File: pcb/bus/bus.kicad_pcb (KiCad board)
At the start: 4 copper layers, 117.4 x 100 mm, 35 parts, among them J201 Conn_02x10_Row_Letter_First, J301 Conn_02x10_Row_Letter_First, J401 Conn_02x10_Row_Letter_First, J501 Conn_02x10_Row_Letter_First, J601 Conn_02x10_Row_Letter_First, J701 Conn_02x10_Row_Letter_First, U101 USBLC6-2SC6, U102 FE1.1s, U103 USBLC6-2SC6, U104 USBLC6-2SC6, U105 USBLC6-2SC6, U106 USBLC6-2SC6, Y101 12MHz

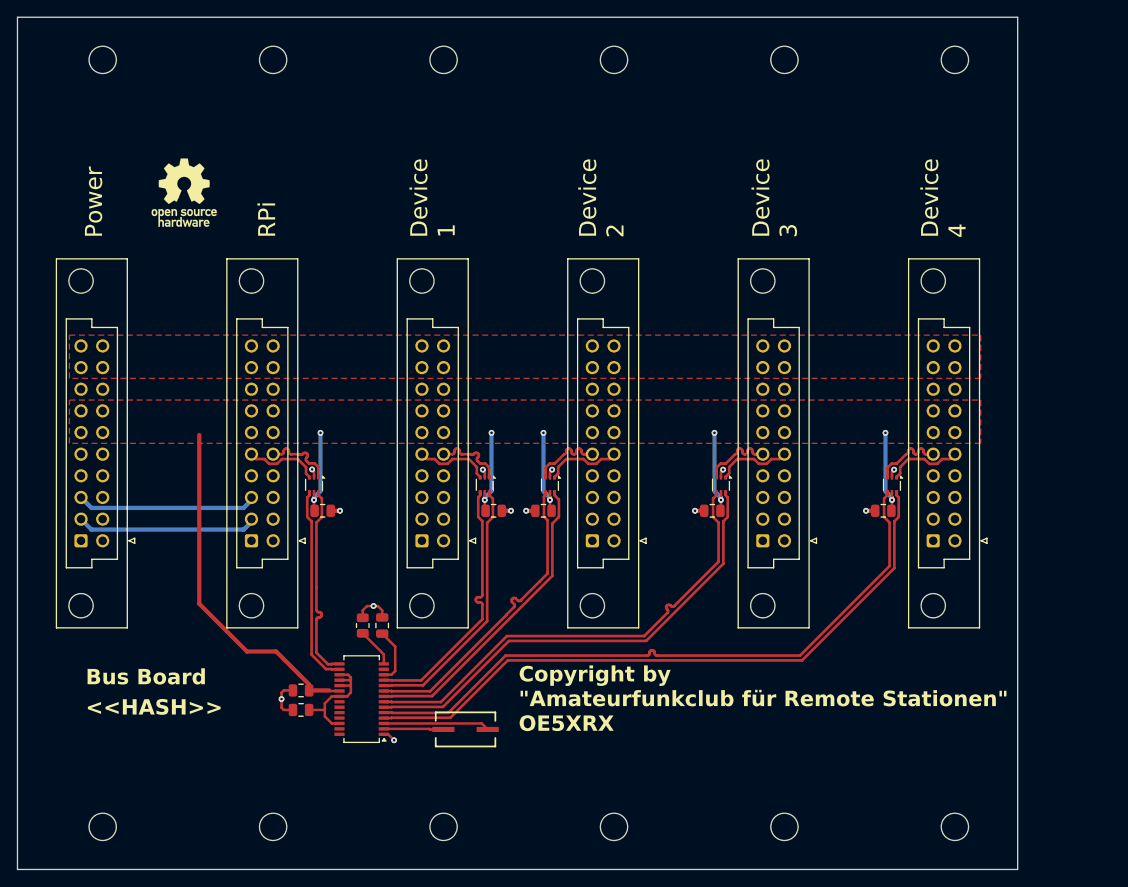
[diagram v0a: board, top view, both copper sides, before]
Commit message: move smd parts to backside - no usb length improvements
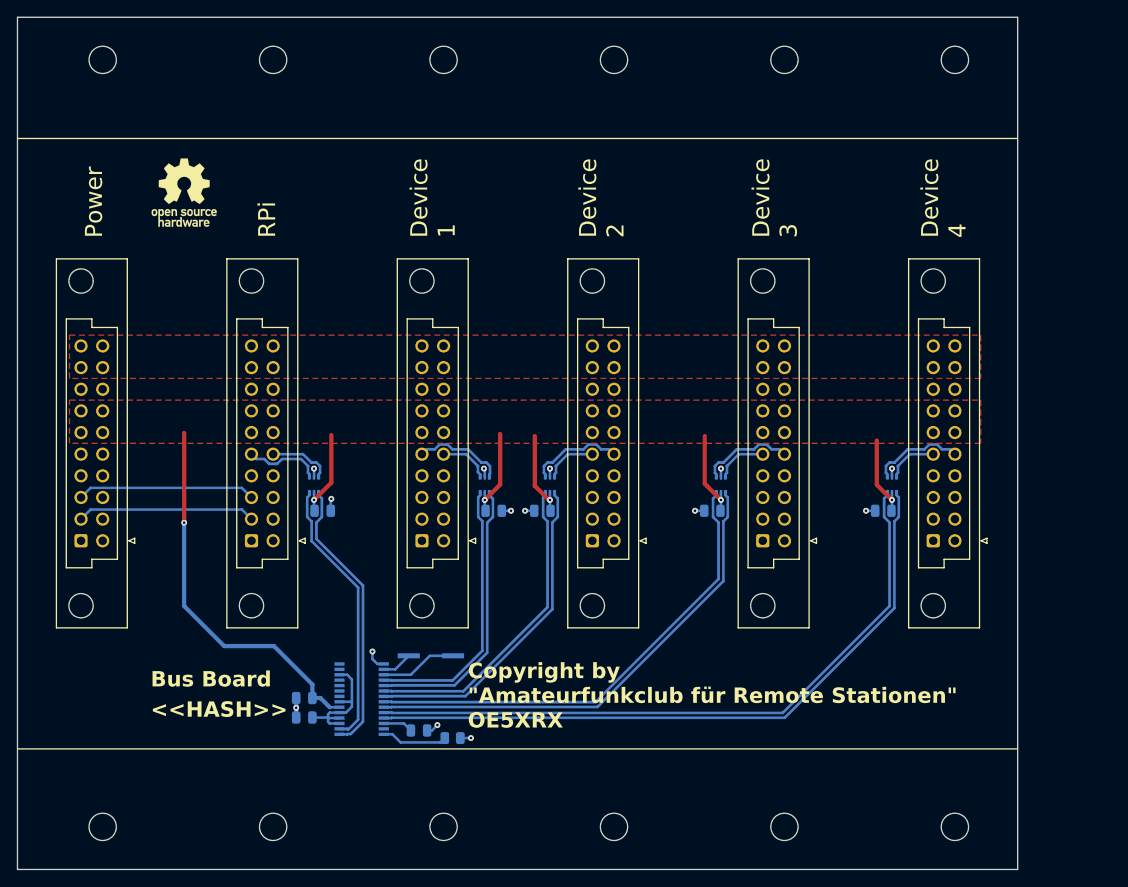
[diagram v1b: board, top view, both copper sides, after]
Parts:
- C101, C102, C103, C104, C105, C106, C107, C108, R103, U101, U102, U103, U104, U105, U106, Y101: moved to B.Cu
- moved R103 16.9 mm to (116.3, 110.0), turned to 0 degrees
- moved C102 13.1 mm to (112.4, 109.1), turned to 0 degrees
- moved Y101 9.54 mm to (113.8, 100.3)
- moved C101 0.97 mm to (98.9, 107.6)
- moved C103 0.97 mm to (98.9, 105.3)
- moved C106 0.13 mm to (126.9, 83.3)
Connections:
- U101 pad 1: /RPI Connector/NS_USB- -> /RPI Connector/NS_USB+
- U101 pad 3: /RPI Connector/NS_USB+ -> /RPI Connector/NS_USB-
- U101 pad 4: /MASTER_USB+ -> /MASTER_USB-
- U101 pad 6: /MASTER_USB- -> /MASTER_USB+
- U102 pad 10: /USB1- -> /USB4-
- U102 pad 11: /USB1+ -> /USB4+
- U102 pad 4: /USB4- -> /USB1-
- U102 pad 5: /USB4+ -> /USB1+
- U102 pad 6: /USB3- -> /USB2-
- U102 pad 7: /USB3+ -> /USB2+
- U102 pad 8: /USB2- -> /USB3-
- U102 pad 9: /USB2+ -> /USB3+
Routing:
- net /MASTER_USB-: track 23.3 -> 33.0 mm
- net /MASTER_USB+: track 23.4 -> 32.0 mm
- net +5V: track 89.9 -> 96.4 mm, vias 10 -> 6
- net Net-(U102-XIN): track 12.5 -> 9.05 mm
- net Net-(U102-XOUT): track 7.02 -> 3.59 mm
- net Net-(U102-REXT): track 4.71 -> 7.76 mm
- net /VD18: track 6.54 -> 3.52 mm
- net /Device Connector 1/NS_USB-: track 8.90 -> 6.08 mm
- net /USB4+: track 76.4 -> 79.2 mm
- net /Device Connector 2/NS_USB+: track 8.98 -> 6.28 mm
- net /Device Connector 3/NS_USB+: track 8.91 -> 6.21 mm
- net /Device Connector 4/NS_USB+: track 8.85 -> 6.15 mm
- net GND: track 20.8 -> 18.2 mm, vias 13 -> 14
- net /USB2+: track 36.0 -> 38.2 mm
- net /Device Connector 4/NS_USB-: track 8.93 -> 11.0 mm
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
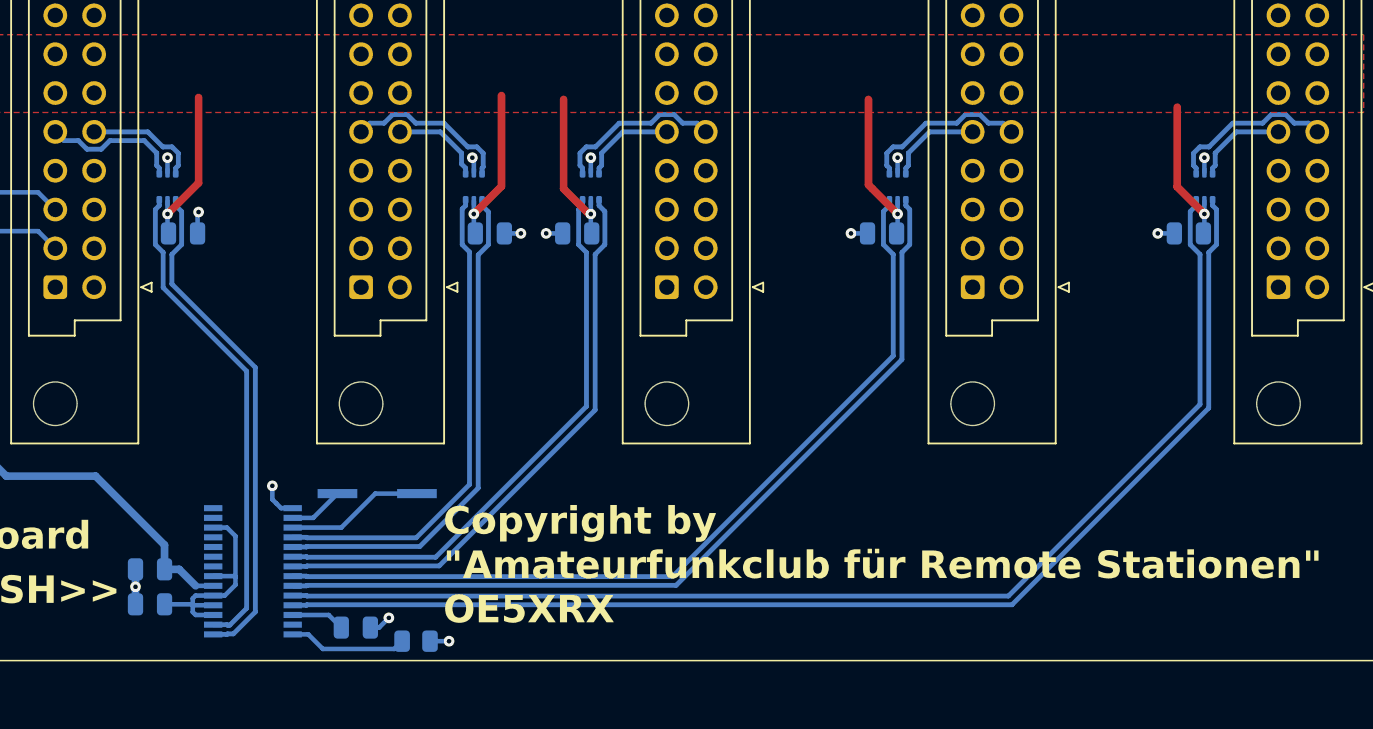
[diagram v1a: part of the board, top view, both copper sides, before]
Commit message: fix diff pair
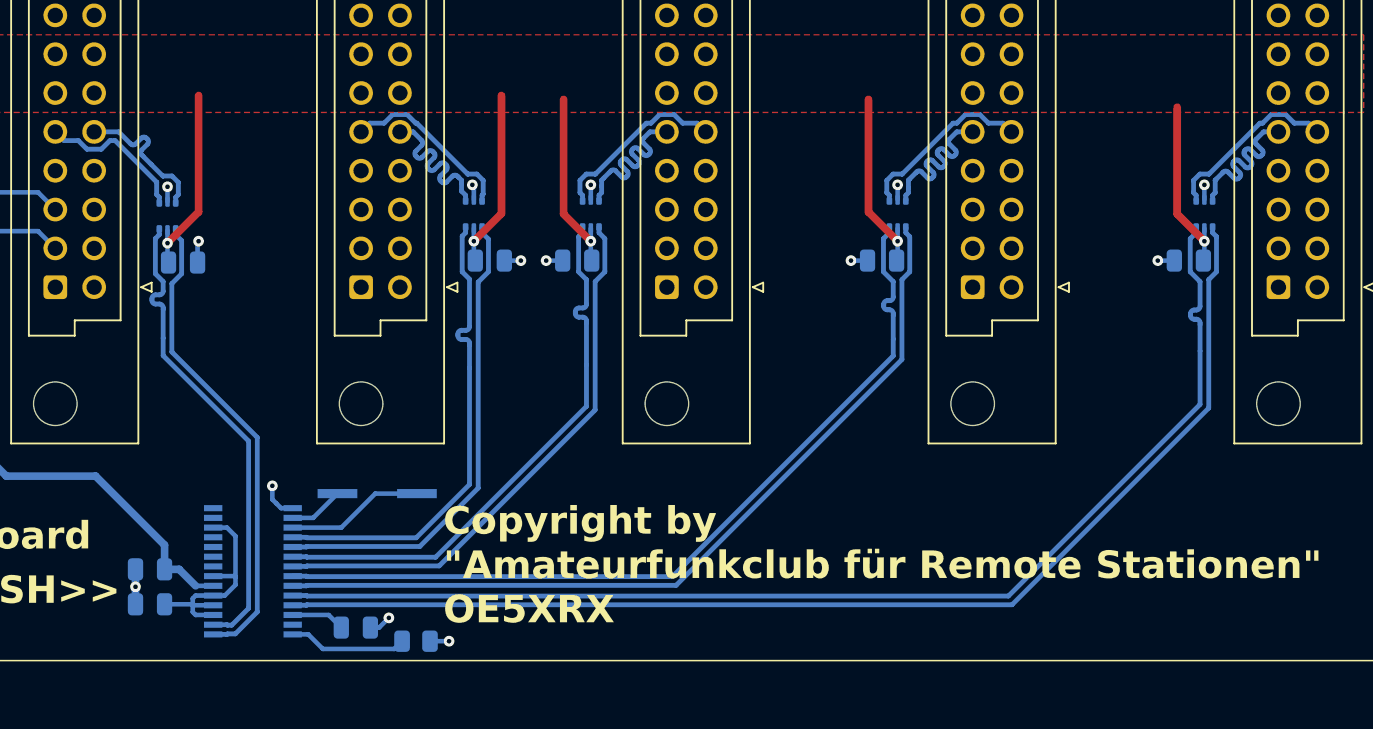
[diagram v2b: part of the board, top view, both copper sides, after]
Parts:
- moved U101 1.91 mm to (100.1, 82.2)
- moved C104 1.90 mm to (101.1, 85.2)
- moved C105 1.78 mm to (121.2, 85.1)
- moved C106 1.78 mm to (126.9, 85.1)
- moved C107 1.78 mm to (146.8, 85.1)
- moved C108 1.78 mm to (166.9, 85.1)
- moved U103 1.78 mm to (120.1, 82.0)
- moved U104 1.78 mm to (127.8, 82.0)
- moved U105 1.78 mm to (147.8, 82.0)
- moved U106 1.78 mm to (167.9, 82.0)
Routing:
- net +5V: track 96.4 -> 105.6 mm
- net /Device Connector 3/NS_USB+: track 6.21 -> 11.7 mm
- net /Device Connector 2/NS_USB+: track 6.28 -> 11.8 mm
- net /Device Connector 4/NS_USB+: track 6.15 -> 11.7 mm
- net /Device Connector 1/NS_USB-: track 6.08 -> 11.5 mm
- net /RPI Connector/NS_USB-: track 7.51 -> 9.86 mm
- net /USB3+: track 56.7 -> 55.0 mm
- net /USB2+: track 38.2 -> 36.4 mm
- net /USB1+: track 33.0 -> 31.3 mm
- net /USB4+: track 79.2 -> 77.4 mm
- net /MASTER_USB-: track 33.0 -> 31.3 mm
- net /USB3-: track 55.9 -> 54.9 mm
- net /USB4-: track 78.4 -> 77.4 mm
- net /RPI Connector/NS_USB+: track 9.11 -> 9.90 mm
- net /USB2-: track 37.1 -> 36.4 mm
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
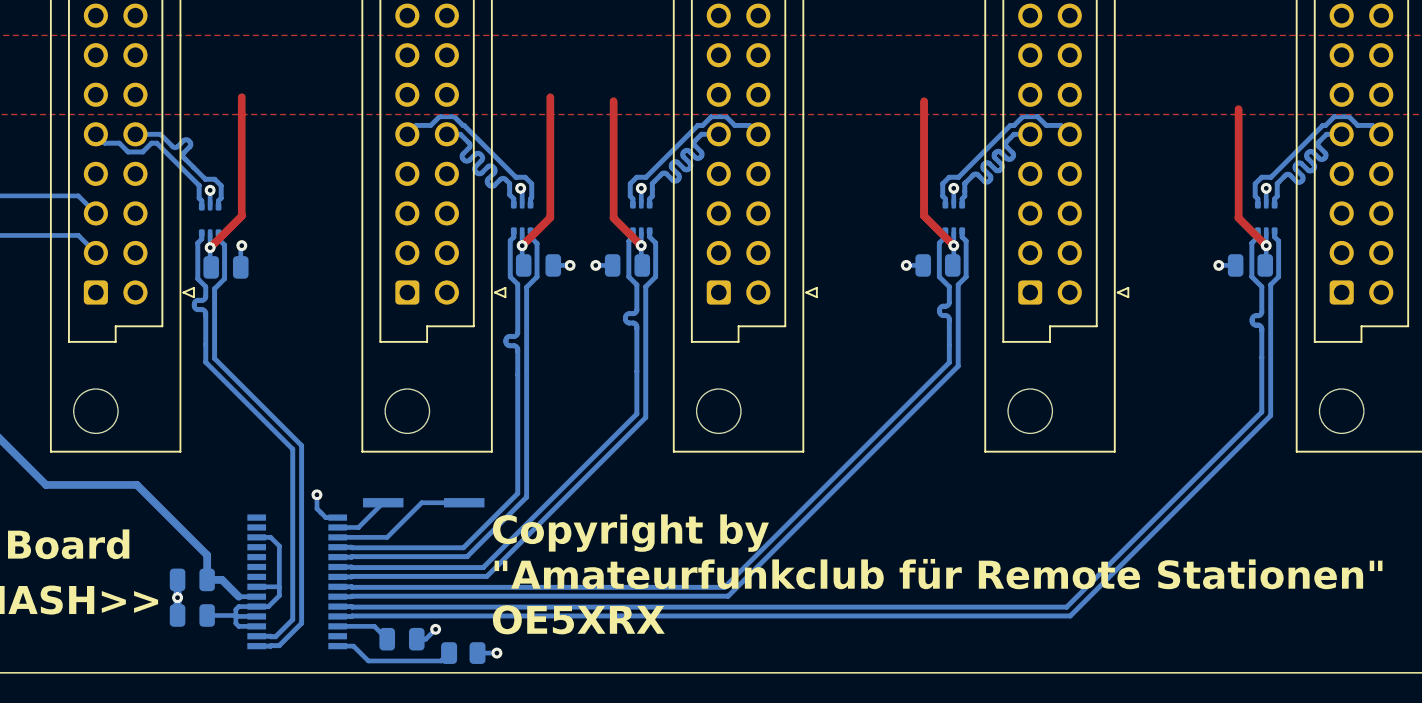
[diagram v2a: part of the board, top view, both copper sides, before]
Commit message: fix footprint in bus pcb
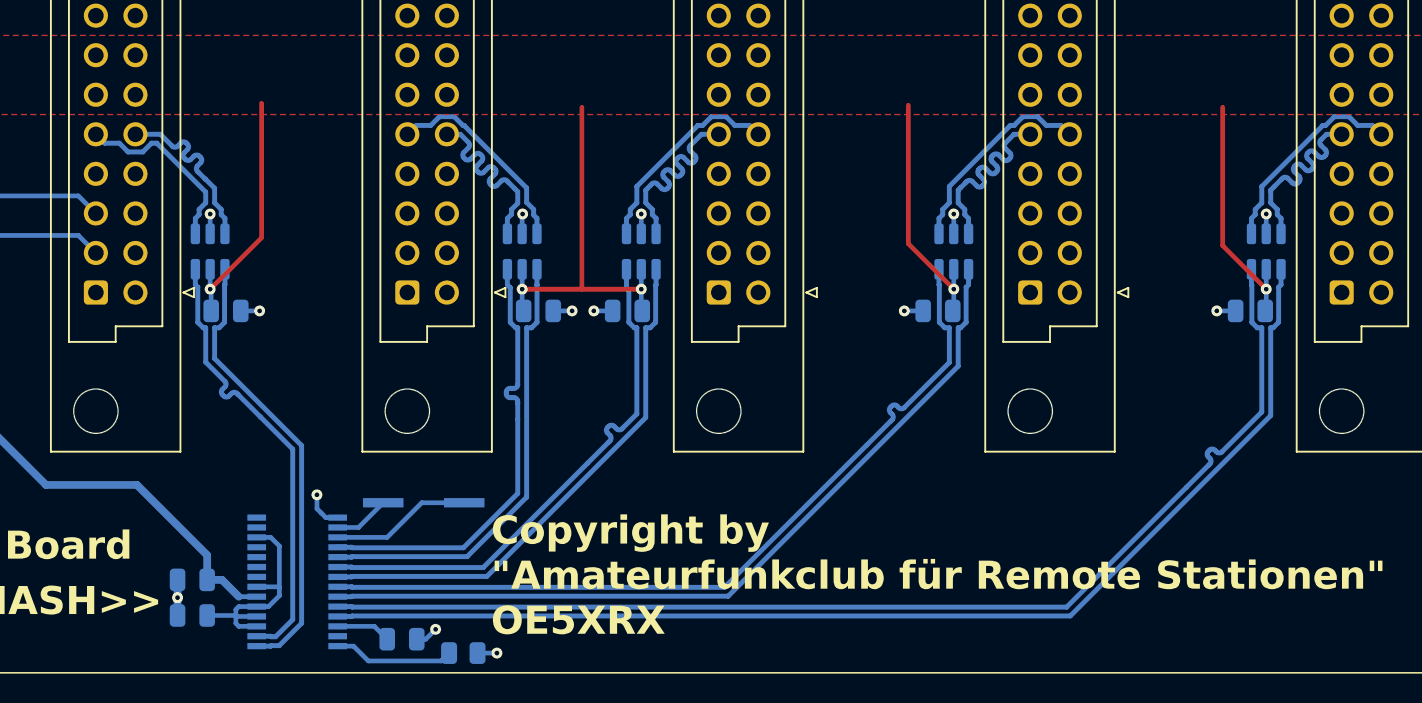
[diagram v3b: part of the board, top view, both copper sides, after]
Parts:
- U101, U103, U104, U105, U106: footprint Package_TO_SOT_SMD:SOT-666 -> Package_TO_SOT_SMD:SOT-23-6
- moved C105 2.92 mm to (121.2, 88.0)
- moved C106 2.92 mm to (126.9, 88.0)
- moved C107 2.92 mm to (146.8, 88.0)
- moved C108 2.92 mm to (166.9, 88.0)
- moved C104 2.79 mm to (101.1, 88.0)
- moved U103 2.16 mm to (120.1, 84.2)
- moved U104 2.16 mm to (127.8, 84.2)
- moved U105 2.16 mm to (147.8, 84.2)
- moved U106 2.16 mm to (167.9, 84.2)
- moved U101 2.03 mm to (100.1, 84.2)
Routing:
- net +5V: track 105.6 -> 116.5 mm
- net /USB1-: track 31.2 -> 28.8 mm
- net /USB1+: track 31.3 -> 28.8 mm
- net /USB2+: track 36.4 -> 34.0 mm
- net /USB2-: track 36.4 -> 33.9 mm
- net /USB4-: track 77.4 -> 75.0 mm
- net /USB4+: track 77.4 -> 75.0 mm
- net /USB3+: track 55.0 -> 52.6 mm
- net /USB3-: track 54.9 -> 52.5 mm
- net /MASTER_USB-: track 31.3 -> 29.0 mm
- net /MASTER_USB+: track 31.2 -> 28.9 mm
- net /RPI Connector/NS_USB+: track 9.90 -> 12.0 mm
- net /RPI Connector/NS_USB-: track 9.86 -> 11.9 mm
- net GND: track 18.2 -> 19.9 mm
- net /Device Connector 1/NS_USB+: track 11.6 -> 13.2 mm
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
